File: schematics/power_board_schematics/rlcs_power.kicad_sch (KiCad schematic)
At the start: 39 parts, among them J1 Conn_01x05_Male, J2 Conn_01x05_Male, J3 UART Conn, J4 Power Board Power Input, J5 Actuator Battery Conn, J6 12v Output, J7 5v Output, J8 Keylock Switch Conn, Q1 Q_NPN_BEC, Q2 Q_NPN_BEC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

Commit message: Fix footprints on Towerside Power Board
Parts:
- J3, J8: footprint TerminalBlock_Phoenix:TerminalBlock_Phoenix_PT-1,5-2-5.0-H_1x02_P5.00mm_Horizontal -> TerminalBlock_Phoenix:TerminalBlock_Phoenix_MPT-0,5-2-2.54_1x02_P2.54mm_Horizontal
- J4: footprint (none) -> TerminalBlock_Phoenix:TerminalBlock_Phoenix_MKDS-1,5-2-5.08_1x02_P5.08mm_Horizontal
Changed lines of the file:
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@@
       (effects (font (size 1.27 1.27)) (justify left))
     )
-    (property "Footprint" "TerminalBlock_Phoenix:TerminalBlock_Phoenix_PT-1,5-2-5.0-H_1x02_P5.00mm_Horizontal" (id 2) (at 168.275 24.13 0)
+    (property "Footprint" "TerminalBlock_Phoenix:TerminalBlock_Phoenix_MPT-0,5-2-2.54_1x02_P2.54mm_Horizontal" (id 2) (at 168.275 24.13 0)
       (effects (font (size 1.27 1.27)) hide)
     )
@@
   (symbol (lib_id "power:+12V") (at 203.2 120.015 0) (unit 1)
     (in_bom yes) (on_board yes)
-    (property "Reference" "#PWR?" (id 0) (at 203.2 123.825 0)
+    (property "Reference" "#PWR0111" (id 0) (at 203.2 123.825 0)
       (effects (font (size 1.27 1.27)) hide)
     )
@@
   (symbol (lib_id "power:+5V") (at 198.12 120.015 0) (unit 1)
     (in_bom yes) (on_board yes)
-    (property "Reference" "#PWR?" (id 0) (at 198.12 123.825 0)
+    (property "Reference" "#PWR0112" (id 0) (at 198.12 123.825 0)
       (effects (font (size 1.27 1.27)) hide)
     )
@@
   (symbol (lib_id "power:GND") (at 111.76 49.53 0) (unit 1)
     (in_bom yes) (on_board yes)
-    (property "Reference" "#PWR?" (id 0) (at 111.76 55.88 0)
+    (property "Reference" "#PWR0110" (id 0) (at 111.76 55.88 0)
       (effects (font (size 1.27 1.27)) hide)
     )
@@
   (symbol (lib_id "power:GND") (at 99.06 174.625 0) (unit 1)
     (in_bom yes) (on_board yes) (fields_autoplaced)
-    (property "Reference" "#PWR?" (id 0) (at 99.06 180.975 0)
+    (property "Reference" "#PWR0107" (id 0) (at 99.06 180.975 0)
       (effects (font (size 1.27 1.27)) hide)
     )
@@
   (symbol (lib_id "power:+12V") (at 186.69 147.955 0) (unit 1)
     (in_bom yes) (on_board yes)
-    (property "Reference" "#PWR?" (id 0) (at 186.69 151.765 0)
+    (property "Reference" "#PWR0105" (id 0) (at 186.69 151.765 0)
       (effects (font (size 1.27 1.27)) hide)
     )
@@
   (symbol (lib_id "power:+5V") (at 181.61 147.955 0) (unit 1)
     (in_bom yes) (on_board yes)
-    (property "Reference" "#PWR?" (id 0) (at 181.61 151.765 0)
+    (property "Reference" "#PWR0104" (id 0) (at 181.61 151.765 0)
       (effects (font (size 1.27 1.27)) hide)
     )
@@
   (symbol (lib_id "power:+5V") (at 109.22 166.37 0) (unit 1)
     (in_bom yes) (on_board yes)
-    (property "Reference" "#PWR?" (id 0) (at 109.22 170.18 0)
+    (property "Reference" "#PWR0108" (id 0) (at 109.22 170.18 0)
       (effects (font (size 1.27 1.27)) hide)
     )
@@
     (property "Reference" "J3" (id 0) (at 143.51 45.72 0))
     (property "Value" "UART Conn" (id 1) (at 143.51 47.625 0))
-    (property "Footprint" "TerminalBlock_Phoenix:TerminalBlock_Phoenix_PT-1,5-2-5.0-H_1x02_P5.00mm_Horizontal" (id 2) (at 143.51 50.165 0)
+    (property "Footprint" "TerminalBlock_Phoenix:TerminalBlock_Phoenix_MPT-0,5-2-2.54_1x02_P2.54mm_Horizontal" (id 2) (at 143.51 50.165 0)
       (effects (font (size 1.27 1.27)) hide)
     )
@@
   (symbol (lib_id "power:GND") (at 178.435 156.21 0) (unit 1)
     (in_bom yes) (on_board yes)
-    (property "Reference" "#PWR?" (id 0) (at 178.435 162.56 0)
+    (property "Reference" "#PWR0106" (id 0) (at 178.435 162.56 0)
       (effects (font (size 1.27 1.27)) hide)
     )
@@
     (property "Reference" "J4" (id 0) (at 37.465 33.02 0))
     (property "Value" "Power Board Power Input" (id 1) (at 37.465 35.56 0))
-    (property "Footprint" "" (id 2) (at 37.465 39.37 0)
+    (property "Footprint" "TerminalBlock_Phoenix:TerminalBlock_Phoenix_MKDS-1,5-2-5.08_1x02_P5.08mm_Horizontal" (id 2) (at 37.465 39.37 0)
       (effects (font (size 1.27 1.27)) hide)
     )
@@
   (symbol (lib_id "power:GND") (at 81.28 49.53 0) (unit 1)
     (in_bom yes) (on_board yes)
-    (property "Reference" "#PWR?" (id 0) (at 81.28 55.88 0)
+    (property "Reference" "#PWR0109" (id 0) (at 81.28 55.88 0)
       (effects (font (size 1.27 1.27)) hide)
     )
@@
       (reference "#PWR0103") (unit 1) (value "GND") (footprint "")
     )
+    (path "/c762348e-1a19-4831-b4a6-db76f55aa092"
+      (reference "#PWR0104") (unit 1) (value "+5V") (footprint "")
+    )
+    (path "/b69512f0-5aac-4ca4-bd36-1612ac1577c8"
+      (reference "#PWR0105") (unit 1) (value "+12V") (footprint "")
+    )
+    (path "/e1ea2902-f8a3-4ff9-8f98-ba6e63555add"
+      (reference "#PWR0106") (unit 1) (value "GND") (footprint "")
+    )
+    (path "/44c7b2ec-4fac-4872-a721-0860585c2f35"
+      (reference "#PWR0107") (unit 1) (value "GND") (footprint "")
+    )
+    (path "/d1f415fb-da4c-446f-b604-1af2fc5e6939"
+      (reference "#PWR0108") (unit 1) (value "+5V") (footprint "")
+    )
+    (path "/e54daa95-192c-496f-afed-65172035ee0d"
+      (reference "#PWR0109") (unit 1) (value "GND") (footprint "")
+    )
+    (path "/37f50b8d-196b-45a8-a1d4-556725fa2187"
+      (reference "#PWR0110") (unit 1) (value "GND") (footprint "")
+    )
     (path "/12616afa-dfb4-4b4e-9b6f-97657970d284"
-      (reference "#PWR?") (unit 1) (value "+12V") (footprint "")
+      (reference "#PWR0111") (unit 1) (value "+12V") (footprint "")
     )
     (path "/217cf45e-9355-4e89-a3c7-f8cb8390dc44"
-      (reference "#PWR?") (unit 1) (value "+5V") (footprint "")
-    )
-    (path "/37f50b8d-196b-45a8-a1d4-556725fa2187"
-      (reference "#PWR?") (unit 1) (value "GND") (footprint "")
-    )
-    (path "/44c7b2ec-4fac-4872-a721-0860585c2f35"
-      (reference "#PWR?") (unit 1) (value "GND") (footprint "")
-    )
-    (path "/b69512f0-5aac-4ca4-bd36-1612ac1577c8"
-      (reference "#PWR?") (unit 1) (value "+12V") (footprint "")
-    )
-    (path "/c762348e-1a19-4831-b4a6-db76f55aa092"
-      (reference "#PWR?") (unit 1) (value "+5V") (footprint "")
-    )
-    (path "/d1f415fb-da4c-446f-b604-1af2fc5e6939"
-      (reference "#PWR?") (unit 1) (value "+5V") (footprint "")
-    )
-    (path "/e1ea2902-f8a3-4ff9-8f98-ba6e63555add"
-      (reference "#PWR?") (unit 1) (value "GND") (footprint "")
-    )
-    (path "/e54daa95-192c-496f-afed-65172035ee0d"
-      (reference "#PWR?") (unit 1) (value "GND") (footprint "")
+      (reference "#PWR0112") (unit 1) (value "+5V") (footprint "")
     )
     (path "/00000000-0000-0000-0000-000059c5bada"
@@
     )
     (path "/dd654b78-9c0d-41b7-ad5c-a9ae8bc2ff19"
-      (reference "J3") (unit 1) (value "UART Conn") (footprint "TerminalBlock_Phoenix:TerminalBlock_Phoenix_PT-1,5-2-5.0-H_1x02_P5.00mm_Horizontal")
+      (reference "J3") (unit 1) (value "UART Conn") (footprint "TerminalBlock_Phoenix:TerminalBlock_Phoenix_MPT-0,5-2-2.54_1x02_P2.54mm_Horizontal")
     )
     (path "/e3210621-2453-4b97-995b-7e62372fc5ce"
-      (reference "J4") (unit 1) (value "Power Board Power Input") (footprint "")
+      (reference "J4") (unit 1) (value "Power Board Power Input") (footprint "TerminalBlock_Phoenix:TerminalBlock_Phoenix_MKDS-1,5-2-5.08_1x02_P5.08mm_Horizontal")
     )
     (path "/b66cf642-a1dc-4e74-85e6-669f964b45aa"
@@
     )
     (path "/0a81f968-d32d-4e4d-acbd-0519aedcf51c"
-      (reference "J8") (unit 1) (value "Keylock Switch Conn") (footprint "TerminalBlock_Phoenix:TerminalBlock_Phoenix_PT-1,5-2-5.0-H_1x02_P5.00mm_Horizontal")
+      (reference "J8") (unit 1) (value "Keylock Switch Conn") (footprint "TerminalBlock_Phoenix:TerminalBlock_Phoenix_MPT-0,5-2-2.54_1x02_P2.54mm_Horizontal")
     )
     (path "/00000000-0000-0000-0000-000059ca1e66"

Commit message: Update Towerside Power Board PCB layout
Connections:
- net ARD_UART_RX: now also J3.2 (Pin_2); no longer J3.1 (Pin_1)
- net ARD_UART_TX: now also J3.1 (Pin_1); no longer J3.2 (Pin_2)

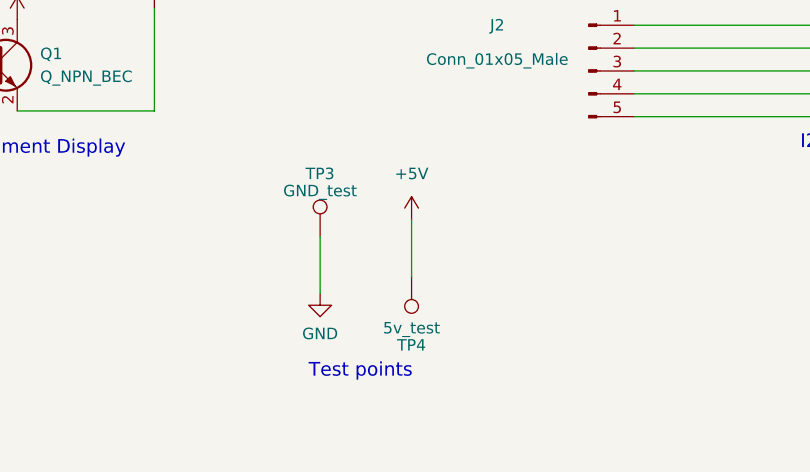
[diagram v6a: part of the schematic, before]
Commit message: Layout Towerside Power Board
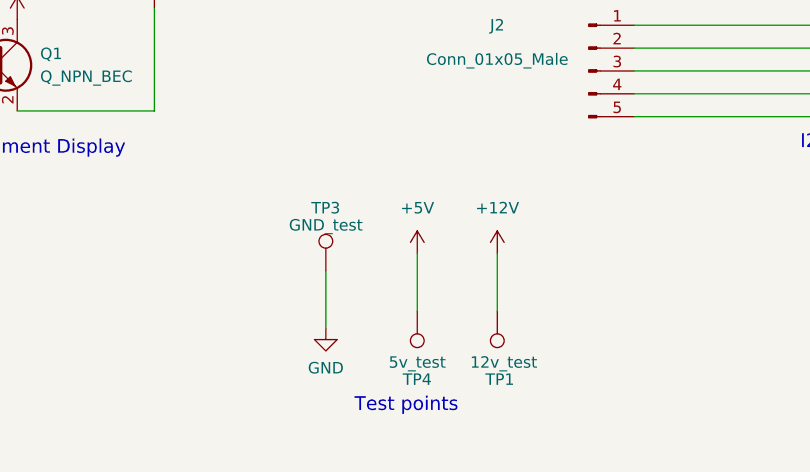
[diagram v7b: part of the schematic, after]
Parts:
- added TP1: 12v_test, Connector_PinSocket_2.00mm:PinSocket_1x01_P2.00mm_Vertical, symbol Connector:TestPoint
- J3, J8: footprint TerminalBlock_Phoenix:TerminalBlock_Phoenix_MPT-0,5-2-2.54_1x02_P2.54mm_Horizontal -> TerminalBlock_TE-Connectivity:TerminalBlock_TE_282834-2_1x02_P2.54mm_Horizontal
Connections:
- net +12V: now also TP1.1
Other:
- moved on the sheet: TP3, TP4
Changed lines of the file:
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@@
+    (stroke (width 0) (type default) (color 0 0 0 0))
+  )
+  (wire (pts (xy 118.745 170.18) (xy 118.745 176.53))
     (stroke (width 0) (type default) (color 0 0 0 0))
   )
@@
     (stroke (width 0) (type default) (color 0 0 0 0))
   )
-  (wire (pts (xy 109.22 166.37) (xy 109.22 172.72))
+  (wire (pts (xy 109.855 170.18) (xy 109.855 176.53))
     (stroke (width 0) (type default) (color 0 0 0 0))
   )
@@
     (stroke (width 0) (type default) (color 0 0 0 0))
   )
-  (wire (pts (xy 99.06 168.275) (xy 99.06 174.625))
+  (wire (pts (xy 99.695 172.085) (xy 99.695 178.435))
     (stroke (width 0) (type default) (color 0 0 0 0))
   )
@@
     (effects (font (size 1.524 1.524)) (justify left bottom))
   )
-  (text "Test points" (at 97.79 184.15 0)
+  (text "Test points" (at 102.87 187.96 0)
     (effects (font (size 1.524 1.524)) (justify left bottom))
   )
@@
     (pin "1")
   )
-  (symbol (lib_id "rlcs_power-rescue:TEST_1P") (at 109.22 172.72 0) (mirror x) (unit 1)
-    (in_bom yes) (on_board yes)
-    (property "Reference" "TP4" (id 0) (at 109.22 180.34 0))
-    (property "Value" "5v_test" (id 1) (at 109.22 178.435 0))
-    (property "Footprint" "Connector_PinSocket_2.00mm:PinSocket_1x01_P2.00mm_Vertical" (id 2) (at 114.3 172.72 0)
-      (effects (font (size 1.27 1.27)) hide)
-    )
-    (property "Datasheet" "" (id 3) (at 114.3 172.72 0)
-      (effects (font (size 1.27 1.27)) hide)
-    )
-    (pin "1")
-  )
-  (symbol (lib_id "rlcs_power-rescue:TEST_1P") (at 99.06 168.275 0) (mirror y) (unit 1)
-    (in_bom yes) (on_board yes)
-    (property "Reference" "TP3" (id 0) (at 99.06 161.29 0))
-    (property "Value" "GND_test" (id 1) (at 99.06 163.195 0))
-    (property "Footprint" "Connector_PinSocket_2.00mm:PinSocket_1x01_P2.00mm_Vertical" (id 2) (at 93.98 168.275 0)
-      (effects (font (size 1.27 1.27)) hide)
-    )
-    (property "Datasheet" "" (id 3) (at 93.98 168.275 0)
+  (symbol (lib_id "rlcs_power-rescue:TEST_1P") (at 109.855 176.53 0) (mirror x) (unit 1)
+    (in_bom yes) (on_board yes)
+    (property "Reference" "TP4" (id 0) (at 109.855 184.15 0))
+    (property "Value" "5v_test" (id 1) (at 109.855 182.245 0))
+    (property "Footprint" "Connector_PinSocket_2.00mm:PinSocket_1x01_P2.00mm_Vertical" (id 2) (at 114.935 176.53 0)
+      (effects (font (size 1.27 1.27)) hide)
+    )
+    (property "Datasheet" "" (id 3) (at 114.935 176.53 0)
+      (effects (font (size 1.27 1.27)) hide)
+    )
+    (pin "1")
+  )
+  (symbol (lib_id "rlcs_power-rescue:TEST_1P") (at 99.695 172.085 0) (mirror y) (unit 1)
+    (in_bom yes) (on_board yes)
+    (property "Reference" "TP3" (id 0) (at 99.695 165.1 0))
+    (property "Value" "GND_test" (id 1) (at 99.695 167.005 0))
+    (property "Footprint" "Connector_PinSocket_2.00mm:PinSocket_1x01_P2.00mm_Vertical" (id 2) (at 94.615 172.085 0)
+      (effects (font (size 1.27 1.27)) hide)
+    )
+    (property "Datasheet" "" (id 3) (at 94.615 172.085 0)
       (effects (font (size 1.27 1.27)) hide)
     )
@@
       (effects (font (size 1.27 1.27)) (justify left))
     )
-    (property "Footprint" "TerminalBlock_Phoenix:TerminalBlock_Phoenix_MPT-0,5-2-2.54_1x02_P2.54mm_Horizontal" (id 2) (at 168.275 24.13 0)
+    (property "Footprint" "TerminalBlock_TE-Connectivity:TerminalBlock_TE_282834-2_1x02_P2.54mm_Horizontal" (id 2) (at 168.275 24.13 0)
       (effects (font (size 1.27 1.27)) hide)
     )
@@
     (pin "2")
   )
-  (symbol (lib_id "power:GND") (at 99.06 174.625 0) (unit 1)
+  (symbol (lib_id "power:GND") (at 99.695 178.435 0) (unit 1)
     (in_bom yes) (on_board yes) (fields_autoplaced)
-    (property "Reference" "#PWR0107" (id 0) (at 99.06 180.975 0)
-      (effects (font (size 1.27 1.27)) hide)
-    )
-    (property "Value" "GND" (id 1) (at 99.06 179.07 0))
-    (property "Footprint" "" (id 2) (at 99.06 174.625 0)
-      (effects (font (size 1.27 1.27)) hide)
-    )
-    (property "Datasheet" "" (id 3) (at 99.06 174.625 0)
+    (property "Reference" "#PWR0107" (id 0) (at 99.695 184.785 0)
+      (effects (font (size 1.27 1.27)) hide)
+    )
+    (property "Value" "GND" (id 1) (at 99.695 182.88 0))
+    (property "Footprint" "" (id 2) (at 99.695 178.435 0)
+      (effects (font (size 1.27 1.27)) hide)
+    )
+    (property "Datasheet" "" (id 3) (at 99.695 178.435 0)
       (effects (font (size 1.27 1.27)) hide)
     )
@@
     )
     (property "Datasheet" "" (id 3) (at 128.905 87.63 0)
+      (effects (font (size 1.27 1.27)) hide)
+    )
+    (pin "1")
+  )
+  (symbol (lib_id "power:+12V") (at 118.745 170.18 0) (unit 1)
+    (in_bom yes) (on_board yes) (fields_autoplaced)
+    (property "Reference" "#PWR03" (id 0) (at 118.745 173.99 0)
+      (effects (font (size 1.27 1.27)) hide)
+    )
+    (property "Value" "+12V" (id 1) (at 118.745 165.1 0))
+    (property "Footprint" "" (id 2) (at 118.745 170.18 0)
+      (effects (font (size 1.27 1.27)) hide)
+    )
+    (property "Datasheet" "" (id 3) (at 118.745 170.18 0)
       (effects (font (size 1.27 1.27)) hide)
     )
@@
     (pin "1")
   )
-  (symbol (lib_id "power:+5V") (at 109.22 166.37 0) (unit 1)
-    (in_bom yes) (on_board yes)
-    (property "Reference" "#PWR0108" (id 0) (at 109.22 170.18 0)
-      (effects (font (size 1.27 1.27)) hide)
-    )
-    (property "Value" "+5V" (id 1) (at 109.22 161.29 0))
-    (property "Footprint" "" (id 2) (at 109.22 166.37 0)
-      (effects (font (size 1.27 1.27)) hide)
-    )
-    (property "Datasheet" "" (id 3) (at 109.22 166.37 0)
+  (symbol (lib_id "power:+5V") (at 109.855 170.18 0) (unit 1)
+    (in_bom yes) (on_board yes)
+    (property "Reference" "#PWR0108" (id 0) (at 109.855 173.99 0)
+      (effects (font (size 1.27 1.27)) hide)
+    )
+    (property "Value" "+5V" (id 1) (at 109.855 165.1 0))
+    (property "Footprint" "" (id 2) (at 109.855 170.18 0)
+      (effects (font (size 1.27 1.27)) hide)
+    )
+    (property "Datasheet" "" (id 3) (at 109.855 170.18 0)
       (effects (font (size 1.27 1.27)) hide)
     )
@@
     (property "Reference" "J3" (id 0) (at 143.51 45.72 0))
     (property "Value" "UART Conn" (id 1) (at 143.51 47.625 0))
-    (property "Footprint" "TerminalBlock_Phoenix:TerminalBlock_Phoenix_MPT-0,5-2-2.54_1x02_P2.54mm_Horizontal" (id 2) (at 143.51 50.165 0)
+    (property "Footprint" "TerminalBlock_TE-Connectivity:TerminalBlock_TE_282834-2_1x02_P2.54mm_Horizontal" (id 2) (at 143.51 50.165 0)
       (effects (font (size 1.27 1.27)) hide)
     )
@@
     )
     (property "Datasheet" "" (id 3) (at 81.28 49.53 0)
+      (effects (font (size 1.27 1.27)) hide)
+    )
+    (pin "1")
+  )
+  (symbol (lib_id "Connector:TestPoint") (at 118.745 176.53 0) (mirror x) (unit 1)
+    (in_bom yes) (on_board yes)
+    (property "Reference" "TP1" (id 0) (at 120.65 184.15 0)
+      (effects (font (size 1.27 1.27)) (justify right))
+    )
+    (property "Value" "12v_test" (id 1) (at 123.19 182.245 0)
+      (effects (font (size 1.27 1.27)) (justify right))
+    )
+    (property "Footprint" "Connector_PinSocket_2.00mm:PinSocket_1x01_P2.00mm_Vertical" (id 2) (at 123.825 176.53 0)
+      (effects (font (size 1.27 1.27)) hide)
+    )
+    (property "Datasheet" "~" (id 3) (at 123.825 176.53 0)
       (effects (font (size 1.27 1.27)) hide)
     )
@@
       (reference "#PWR02") (unit 1) (value "+5V") (footprint "")
     )
+    (path "/99e53eb7-ae07-4739-ab66-0a27060e0339"
+      (reference "#PWR03") (unit 1) (value "+12V") (footprint "")
+    )
     (path "/23aa8bbd-ae0f-48c1-bdc2-39ce4df453b0"
       (reference "#PWR04") (unit 1) (value "+12V") (footprint "")
@@
     )
     (path "/dd654b78-9c0d-41b7-ad5c-a9ae8bc2ff19"
-      (reference "J3") (unit 1) (value "UART Conn") (footprint "TerminalBlock_Phoenix:TerminalBlock_Phoenix_MPT-0,5-2-2.54_1x02_P2.54mm_Horizontal")
+      (reference "J3") (unit 1) (value "UART Conn") (footprint "TerminalBlock_TE-Connectivity:TerminalBlock_TE_282834-2_1x02_P2.54mm_Horizontal")
     )
     (path "/e3210621-2453-4b97-995b-7e62372fc5ce"
@@
     )
     (path "/0a81f968-d32d-4e4d-acbd-0519aedcf51c"
-      (reference "J8") (unit 1) (value "Keylock Switch Conn") (footprint "TerminalBlock_Phoenix:TerminalBlock_Phoenix_MPT-0,5-2-2.54_1x02_P2.54mm_Horizontal")
+      (reference "J8") (unit 1) (value "Keylock Switch Conn") (footprint "TerminalBlock_TE-Connectivity:TerminalBlock_TE_282834-2_1x02_P2.54mm_Horizontal")
     )
     (path "/00000000-0000-0000-0000-000059ca1e66"
@@
       (reference "T2") (unit 1) (value "12 to 5") (footprint "rlcs_power_footprints:VXO78XX-1000")
     )
+    (path "/e952014a-68f6-412c-961a-1e484cff7295"
+      (reference "TP1") (unit 1) (value "12v_test") (footprint "Connector_PinSocket_2.00mm:PinSocket_1x01_P2.00mm_Vertical")
+    )
     (path "/00000000-0000-0000-0000-000059c761f8"
